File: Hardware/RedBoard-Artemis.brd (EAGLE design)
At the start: 68.6 x 58.4 mm, 122 parts, among them IC3 LM1117, J2 CORTEX_DEBUG, J3 POWER_JACKTOE, J5 USB-C, Q1 2.5A/30V/105mΩ, U1 ARTEMIS_MODULESMD, U3 AP2112-3.3V, U5 CH340C, Y1 32.768kHz

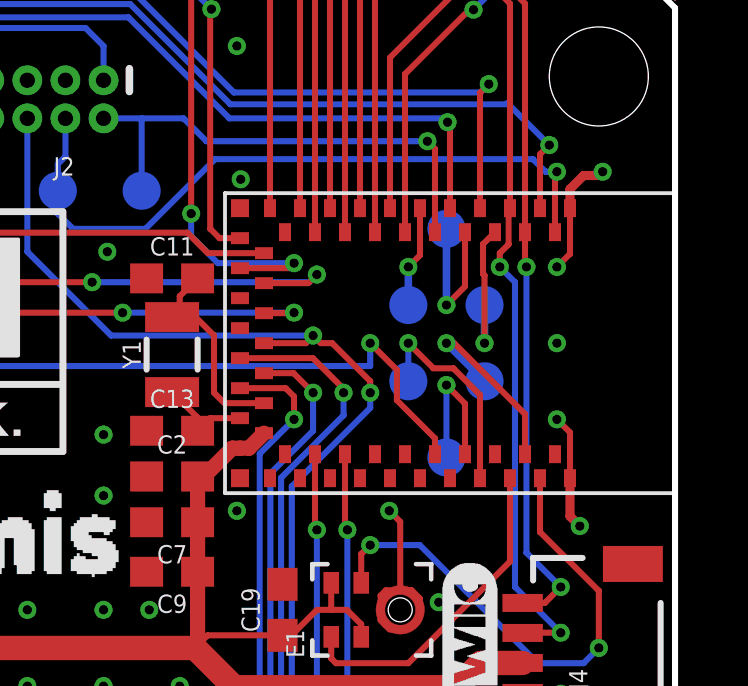
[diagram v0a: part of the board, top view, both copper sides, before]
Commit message: Adding production panels
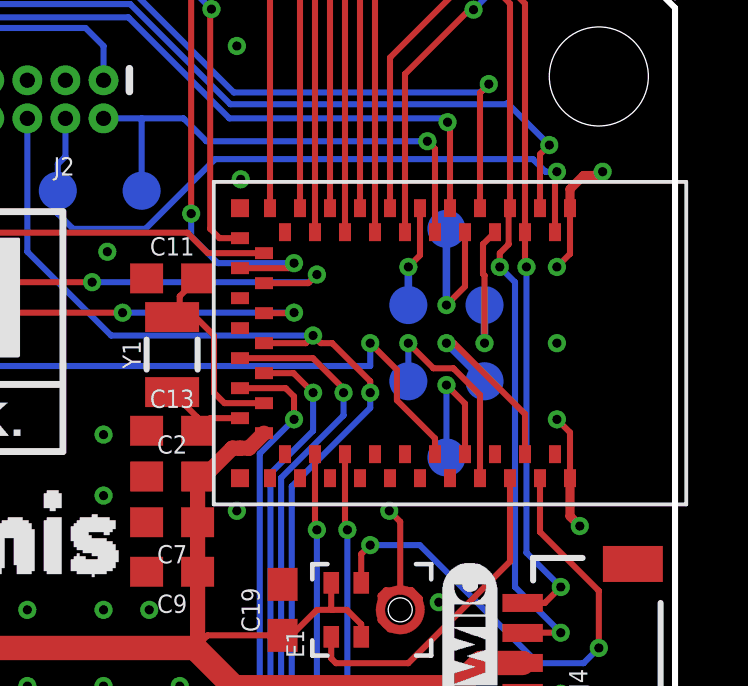
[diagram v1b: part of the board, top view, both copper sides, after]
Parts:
- moved U$49 5.21 mm to (12.7, 50.2), turned to 270 degrees
- moved U$53 5.21 mm to (10.2, 50.2), turned to 270 degrees
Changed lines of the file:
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@@
 <element name="U$71" library="buzzard_labels (2)" package="RX11" value="" x="63.373" y="45.974" smashed="yes" rot="R90"/>
 <element name="U$72" library="buzzard_labels (2)" package="TX10" value="" x="60.96" y="45.847" smashed="yes" rot="R90"/>
-<element name="U$49" library="buzzard_labels (3)" package="RX01" value="" x="12.7" y="44.958" smashed="yes" rot="MR90"/>
-<element name="U$53" library="buzzard_labels (3)" package="TX00" value="" x="10.16" y="44.958" smashed="yes" rot="MR90"/>
+<element name="U$49" library="buzzard_labels (3)" package="RX01" value="" x="12.7" y="50.165" smashed="yes" rot="MR270"/>
+<element name="U$53" library="buzzard_labels (3)" package="TX00" value="" x="10.16" y="50.165" smashed="yes" rot="MR270"/>
 <element name="JP16" library="SparkFun-Jumpers" package="SMT-JUMPER_2_NC_TRACE_SILK" value="" x="24.13" y="46.99" smashed="yes" rot="MR90">
 <attribute name="NAME" x="25.273" y="46.99" size="0.6096" layer="26" font="vector" ratio="20" rot="MR90" align="bottom-center"/>
